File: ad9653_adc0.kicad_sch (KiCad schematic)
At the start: 20 parts, among them J201 142-0701-201, J202 142-0701-201, J203 142-0701-201, J204 142-0701-201, U201 AD9653BCPZ-125

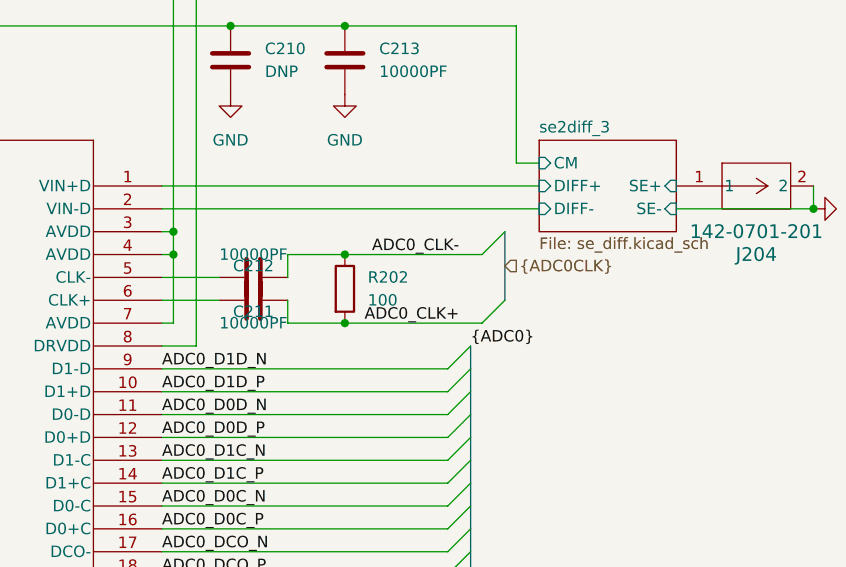
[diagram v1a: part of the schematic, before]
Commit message: fixed differential pair impedance and length matching. Also fixed DRC errors (trace spacing). These are only layout changes, the schematic remains unchanged.
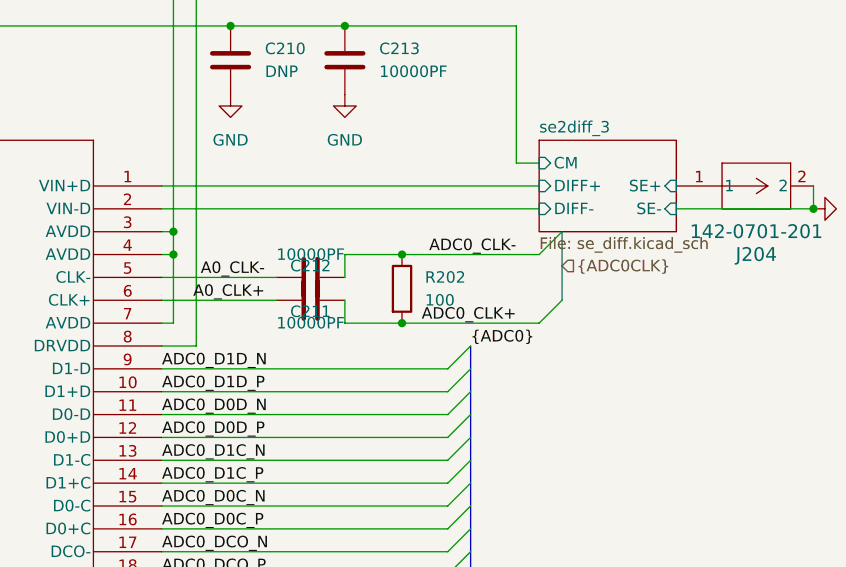
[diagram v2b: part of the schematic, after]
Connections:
- net A0_CLK-: now reaches C211.2, U201.5 (CLK-)
- net A0_CLK+: now reaches C212.2, U201.6 (CLK+)
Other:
- moved on the sheet: C211, C212, R202
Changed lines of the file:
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@@
 	)
 	(junction
-		(at 219.71 91.44)
+		(at 226.06 91.44)
 		(diameter 0)
 		(color 0 0 0 0)
@@
 	)
 	(junction
-		(at 219.71 99.06)
+		(at 226.06 99.06)
 		(diameter 0)
 		(color 0 0 0 0)
@@
 	)
 	(bus_entry
-		(at 237.49 96.52)
+		(at 243.84 96.52)
 		(size -2.54 2.54)
 		(stroke
@@
 	)
 	(bus_entry
-		(at 237.49 88.9)
+		(at 243.84 88.9)
 		(size -2.54 2.54)
 		(stroke
@@
 	(wire
 		(pts
-			(xy 199.39 93.98) (xy 205.74 93.98)
+			(xy 199.39 93.98) (xy 212.09 93.98)
 		)
 		(stroke
@@
 	(wire
 		(pts
-			(xy 213.36 93.98) (xy 213.36 91.44)
+			(xy 219.71 93.98) (xy 219.71 91.44)
 		)
 		(stroke
@@
 	(wire
 		(pts
-			(xy 213.36 91.44) (xy 219.71 91.44)
+			(xy 219.71 91.44) (xy 226.06 91.44)
 		)
 		(stroke
@@
 	(wire
 		(pts
-			(xy 219.71 91.44) (xy 234.95 91.44)
+			(xy 226.06 91.44) (xy 241.3 91.44)
 		)
 		(stroke
@@
 	(wire
 		(pts
-			(xy 199.39 96.52) (xy 205.74 96.52)
+			(xy 199.39 96.52) (xy 212.09 96.52)
 		)
 		(stroke
@@
 	(bus
 		(pts
-			(xy 237.49 88.9) (xy 237.49 96.52)
+			(xy 243.84 88.9) (xy 243.84 96.52)
 		)
 		(stroke
@@
 	(wire
 		(pts
-			(xy 219.71 99.06) (xy 234.95 99.06)
+			(xy 226.06 99.06) (xy 241.3 99.06)
 		)
 		(stroke
@@
 	(wire
 		(pts
-			(xy 213.36 96.52) (xy 213.36 99.06)
+			(xy 219.71 96.52) (xy 219.71 99.06)
 		)
 		(stroke
@@
 	(wire
 		(pts
-			(xy 213.36 99.06) (xy 219.71 99.06)
+			(xy 219.71 99.06) (xy 226.06 99.06)
 		)
 		(stroke
@@
 	)
 	(label "ADC0_CLK+"
-		(at 232.41 99.06 180)
+		(at 238.76 99.06 180)
 		(effects
 			(font
@@
 		)
 	)
+	(label "A0_CLK+"
+		(at 210.82 96.52 180)
+		(effects
+			(font
+				(size 1.27 1.27)
+			)
+			(justify right bottom)
+		)
+	)
 	(label "ADC0_DCO_P"
 		(at 199.39 127 0)
@@
 		)
 	)
+	(label "A0_CLK-"
+		(at 210.82 93.98 180)
+		(effects
+			(font
+				(size 1.27 1.27)
+			)
+			(justify right bottom)
+		)
+	)
 	(label "ADC01_PDWN"
 		(at 128.27 124.46 180)
@@
 	)
 	(label "ADC0_CLK-"
-		(at 232.41 91.44 180)
+		(at 238.76 91.44 180)
 		(effects
 			(font
@@
 	(hierarchical_label "{ADC0CLK}"
 		(shape input)
-		(at 237.49 92.71 0)
+		(at 243.84 92.71 0)
 		(effects
 			(font
@@
 	(symbol
 		(lib_id "Device:C")
-		(at 209.55 93.98 270)
+		(at 215.9 93.98 270)
 		(unit 1)
 		(body_style 1)
@@
 		(dnp no)
 		(property "Reference" "C211"
-			(at 209.55 97.79 90)
+			(at 215.9 97.79 90)
 			(show_name no)
 			(do_not_autoplace no)
@@
 		)
 		(property "Value" "10000PF"
-			(at 209.55 99.06 90)
+			(at 215.9 99.06 90)
 			(show_name no)
 			(do_not_autoplace no)
@@
 		)
 		(property "Footprint" "Capacitor_SMD:C_0603_1608Metric"
-			(at 205.74 94.9452 0)
+			(at 212.09 94.9452 0)
 			(hide yes)
 			(show_name no)
@@
 		)
 		(property "Datasheet" ""
-			(at 209.55 93.98 0)
+			(at 215.9 93.98 0)
 			(hide yes)
 			(show_name no)
@@
 		)
 		(property "Description" "Unpolarized capacitor"
-			(at 209.55 93.98 0)
+			(at 215.9 93.98 0)
 			(hide yes)
 			(show_name no)
@@
 		)
 		(property "Vendor" "digikey:445-2664-1-ND"
-			(at 115.57 -115.57 0)
+			(at 121.92 -115.57 0)
 			(hide yes)
 			(show_name no)
@@
 	(symbol
 		(lib_id "Device:C")
-		(at 209.55 96.52 270)
+		(at 215.9 96.52 270)
 		(mirror x)
 		(unit 1)
@@
 		(dnp no)
 		(property "Reference" "C212"
-			(at 209.55 92.71 90)
+			(at 215.9 92.71 90)
 			(show_name no)
 			(do_not_autoplace no)
@@
 		)
 		(property "Value" "10000PF"
-			(at 209.55 91.44 90)
+			(at 215.9 91.44 90)
 			(show_name no)
 			(do_not_autoplace no)
@@
 		)
 		(property "Footprint" "Capacitor_SMD:C_0603_1608Metric"
-			(at 205.74 95.5548 0)
+			(at 212.09 95.5548 0)
 			(hide yes)
 			(show_name no)
@@
 		)
 		(property "Datasheet" ""
-			(at 209.55 96.52 0)
+			(at 215.9 96.52 0)
 			(hide yes)
 			(show_name no)
@@
 		)
 		(property "Description" "Unpolarized capacitor"
-			(at 209.55 96.52 0)
+			(at 215.9 96.52 0)
 			(hide yes)
 			(show_name no)
@@
 		)
 		(property "Vendor" "digikey:445-2664-1-ND"
-			(at 113.03 306.07 0)
+			(at 119.38 306.07 0)
 			(hide yes)
 			(show_name no)
@@
 	(symbol
 		(lib_id "Device:R")
-		(at 219.71 95.25 0)
+		(at 226.06 95.25 0)
 		(unit 1)
 		(body_style 1)
@@
 		(fields_autoplaced yes)
 		(property "Reference" "R202"
-			(at 222.25 93.9799 0)
+			(at 228.6 93.9799 0)
 			(show_name no)
 			(do_not_autoplace no)
@@
 		)
 		(property "Value" "100"
-			(at 222.25 96.5199 0)
+			(at 228.6 96.5199 0)
 			(show_name no)
 			(do_not_autoplace no)
@@
 		)
 		(property "Footprint" "Resistor_SMD:R_0603_1608Metric"
-			(at 217.932 95.25 90)
+			(at 224.282 95.25 90)
 			(hide yes)
 			(show_name no)
@@
 		)
 		(property "Datasheet" ""
-			(at 219.71 95.25 0)
+			(at 226.06 95.25 0)
 			(hide yes)
 			(show_name no)
@@
 		)
 		(property "Description" "Resistor"
-			(at 219.71 95.25 0)
+			(at 226.06 95.25 0)
 			(hide yes)
 			(show_name no)
@@
 		)
 		(property "Vendor" "digikey:311-100HRCT-ND"
-			(at 0 190.5 0)
+			(at 6.35 190.5 0)
 			(hide yes)
 			(show_name no)
